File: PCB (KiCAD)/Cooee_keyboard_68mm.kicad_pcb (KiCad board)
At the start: 2 copper layers, 66.8 x 41.8 mm, 109 parts, among them J9 Conn_01x05_Pin, U1 TCA8418RTWR

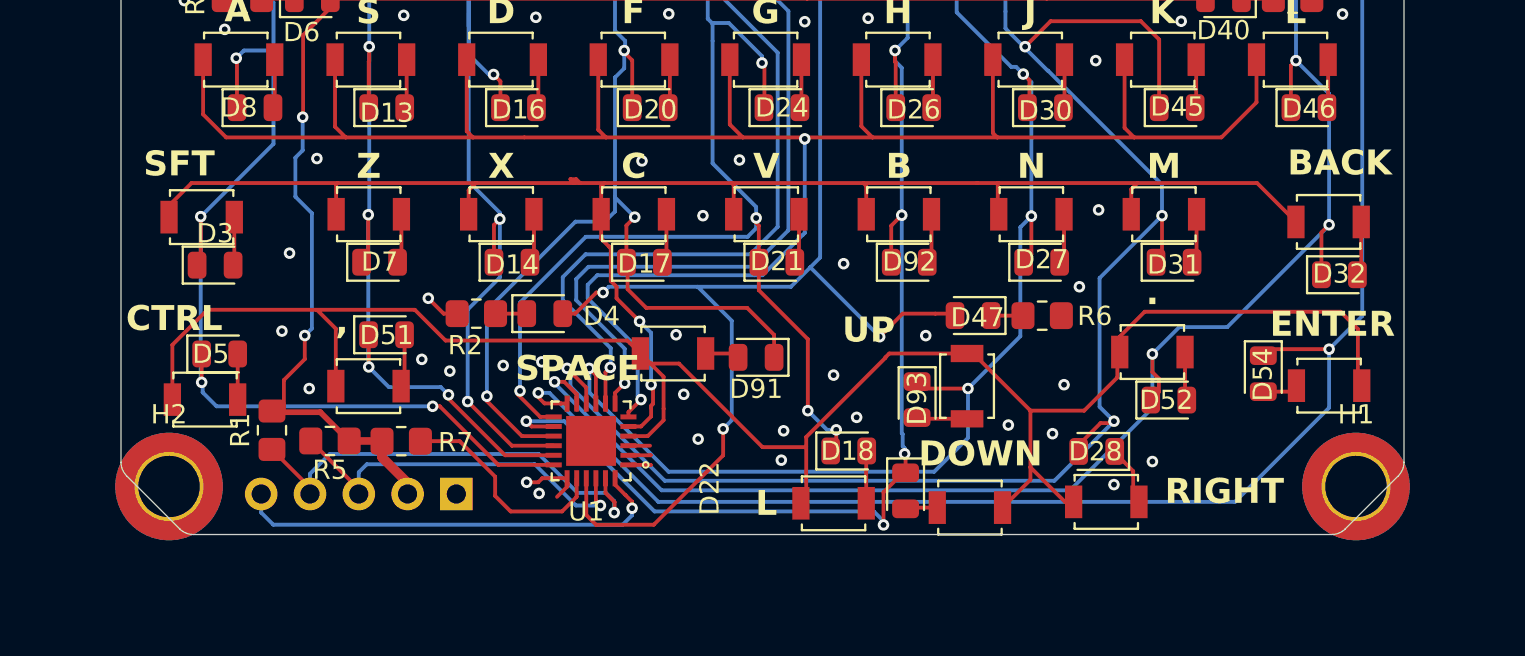
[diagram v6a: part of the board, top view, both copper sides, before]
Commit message: centred the USB port and screen properly
centred the USB port and screen properly. trying to implement compressed audio over radio but compression function started throwing stack overflow
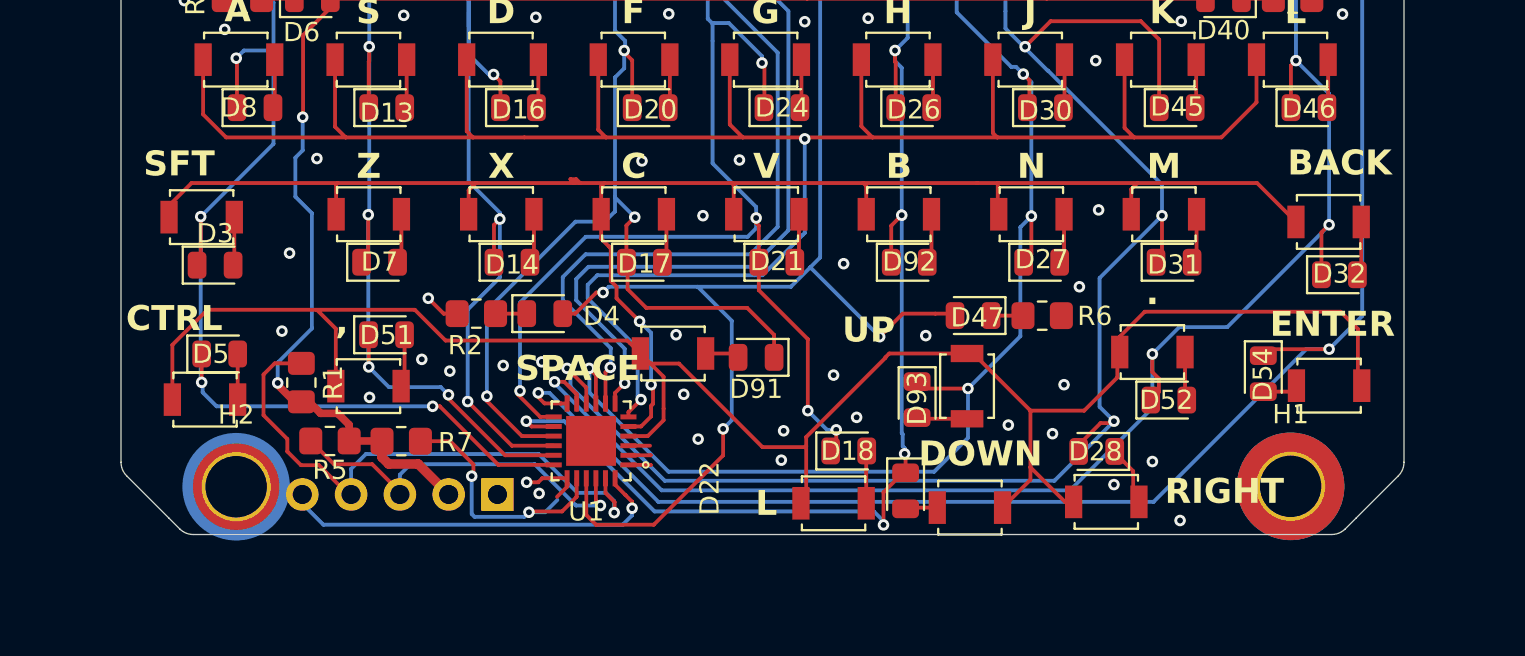
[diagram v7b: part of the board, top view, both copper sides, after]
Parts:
- added ?: , , F.Cu at (122.8, 117.7)
- moved H2 3.50 mm to (122.8, 117.7)
- moved H1 3.40 mm to (177.7, 117.7)
- moved R1 2.91 mm to (126.2, 112.3), turned to -90 degrees
- moved J9 2.14 mm to (136.4, 118.1)
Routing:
- net KEEB_SCL: track 24.3 -> 30.4 mm
- net KEEB_RST: track 11.5 -> 14.7 mm, vias 0 -> 2
- net KEEB_INT: track 23.7 -> 20.9 mm
- net +3.3V: track 140.1 -> 142.0 mm
- net COL1: track 88.1 -> 86.3 mm
- net GND: track 67.0 -> 67.9 mm, vias 59 -> 60

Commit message: pcb work
pcb work
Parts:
- moved D22 4.30 mm to (161.4, 115.8), turned to 180 degrees
- moved D5 2.85 mm to (121.3, 113.6)
- moved SWe12 2.75 mm to (122.0, 110.5)
- moved D18 2.39 mm to (157.1, 116.1)
- moved SWe13 2.39 mm to (156.3, 118.8)
- moved D28 1.50 mm to (166.1, 116.2)
- moved SWe7 1.50 mm to (166.6, 118.8)
- moved SWe50 1.47 mm to (179.5, 111.0)
- moved D54 0.83 mm to (176.0, 111.1)
- moved SWe88 0.72 mm to (161.5, 112.2)
- moved D39 0.66 mm to (180.8, 82.2)
- moved SWe29 0.66 mm to (180.5, 79.7)
- moved D2 0.55 mm to (120.6, 82.4)
- moved ESC1 0.55 mm to (119.8, 79.9)
- moved D38 0.54 mm to (174.4, 82.3)
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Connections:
- ? pad 1: (no net) -> GND
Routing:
- net GND: track 67.9 -> 85.0 mm
- net COL6: track 74.7 -> 80.8 mm, vias 7 -> 8
- net ROW5: track 101.4 -> 97.3 mm
- net KEEB_RST: track 14.7 -> 13.0 mm, vias 2 -> 0
- net COL1: track 86.3 -> 88.0 mm
- net Net-(D22-A): track 1.68 -> 3.28 mm
- net COL3: track 98.9 -> 97.3 mm
- net ROW1: track 148.7 -> 147.2 mm
- net COL5: track 70.7 -> 72.2 mm
- net Net-(D5-A): track 2.38 -> 3.62 mm
- net COL10: track 69.4 -> 70.3 mm
- net Net-(D28-K): track 2.24 -> 3.15 mm
- net COL9: track 56.4 -> 55.6 mm
- net +3.3V: track 142.0 -> 142.8 mm
- net Net-(D93-A): track 2.63 -> 3.30 mm
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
